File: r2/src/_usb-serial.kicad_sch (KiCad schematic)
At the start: 8 parts

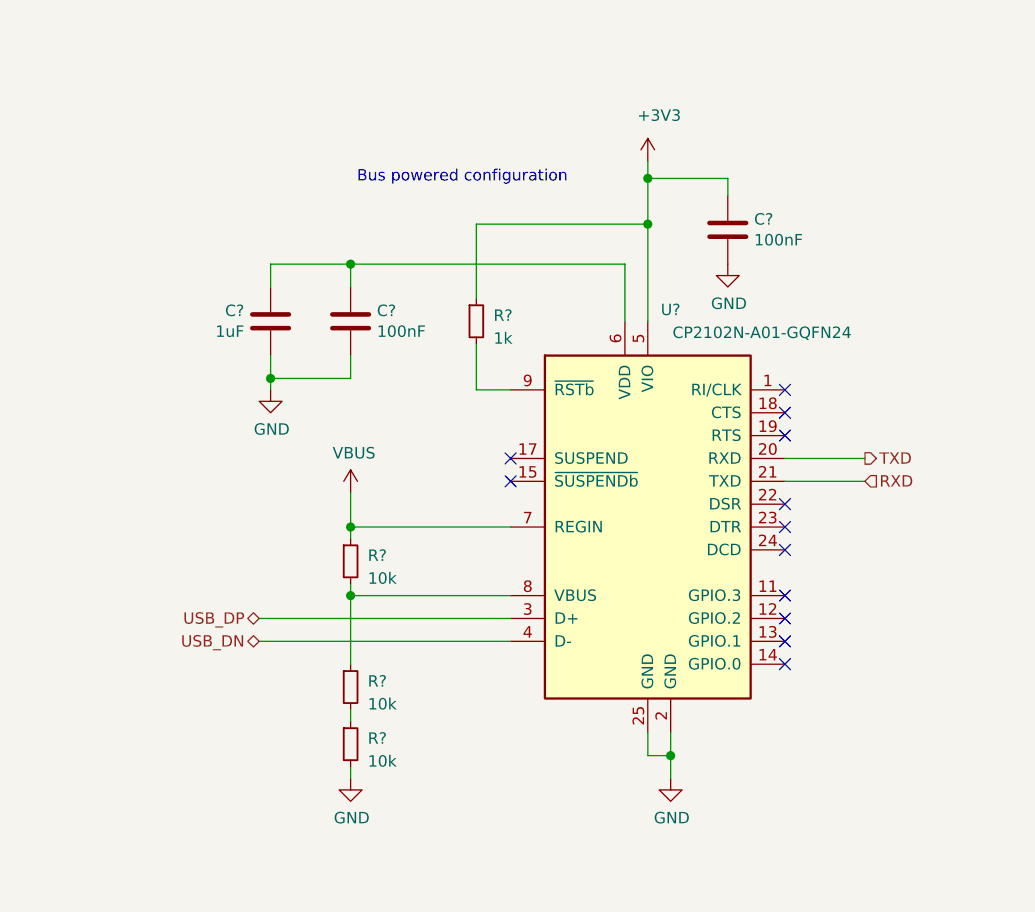
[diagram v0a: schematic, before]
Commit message: Annotate schematic, ERC pass
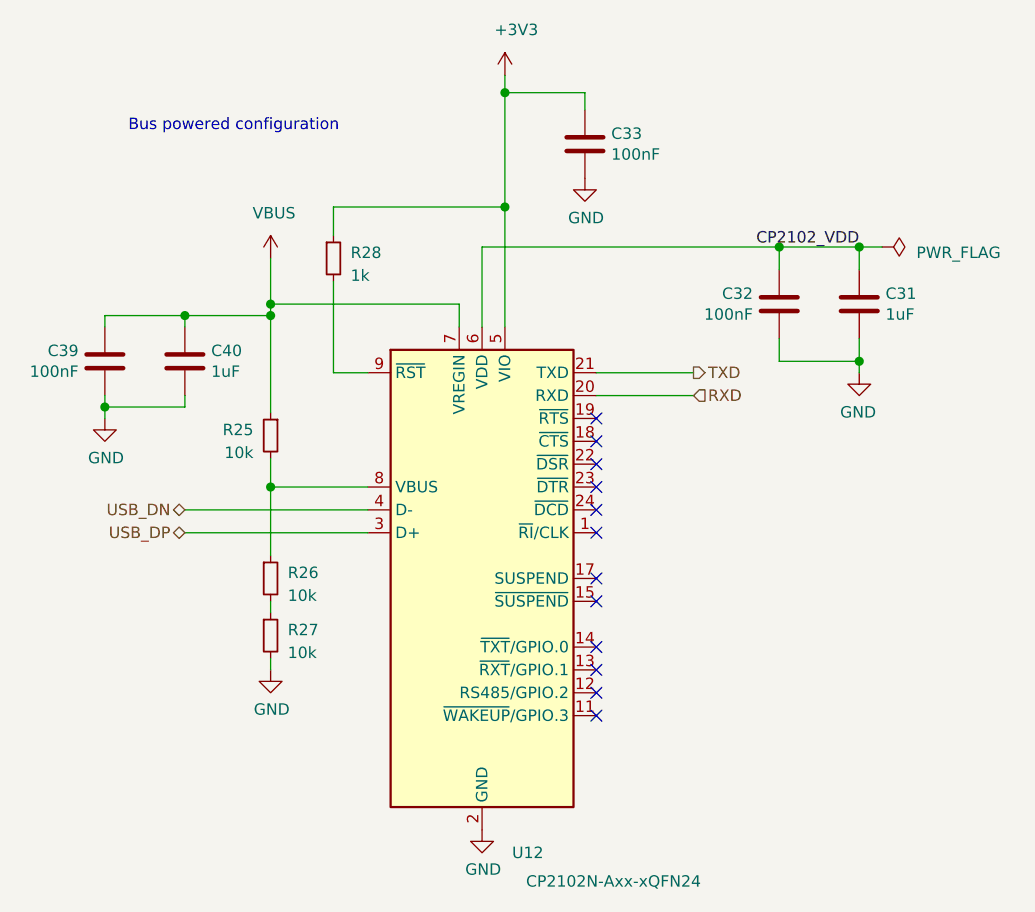
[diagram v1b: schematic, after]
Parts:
- removed U?: CP2102N-A01-GQFN24, Package_DFN_QFN:QFN-24-1EP_4x4mm_P0.5mm_EP2.6x2.6mm, symbol Interface_USB:CP2102N-A01-GQFN24
- added C39: 100nF, Capacitor_SMD:C_0402_1005Metric, symbol Device:C
- added C40: 1uF, Capacitor_SMD:C_0603_1608Metric, symbol Device:C
- added U12: CP2102N-Axx-xQFN24, Package_DFN_QFN:QFN-24-1EP_4x4mm_P0.5mm_EP2.6x2.6mm, symbol Interface_USB:CP2102N-Axx-xQFN24
- gave numbers to parts that had none: 7
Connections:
- net +3V3: now also U12.5 (VIO)
- net GND: now also C39.2, C40.2, U12.2 (GND), U12.25 (GND)
- net RXD: now also U12.20 (RXD)
- net TXD: now also U12.21 (TXD)
- net USB_DN: now also U12.4 (D-)
- net USB_DP: now also U12.3 (D+)
- net VBUS: now also C39.1, C40.1, U12.7 (VREGIN)
- net CP2102_VDD: now reaches C31.1, C32.1
- net CP2102_VDD: now also U12.6 (VDD)
- net at R25.2, R26.1: now also U12.8 (VBUS)
- net at R28.2: now also U12.9 (~RST)
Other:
- moved on the sheet: C31, C32, C33, R25, R26, R27, R28

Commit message: Most footprints assigned
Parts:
- C32, C33, C39: footprint Capacitor_SMD:C_0402_1005Metric -> Capacitor_SMD:C_0603_1608Metric
- R25, R26, R27: value 10k -> 23.7k; footprint (none) -> Resistor_SMD:R_0603_1608Metric
- R28: footprint (none) -> Resistor_SMD:R_0603_1608Metric
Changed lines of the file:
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@@
     (pin "1")
   )
-  (symbol (lib_id "Device:R_Small") (at 119.38 93.98 0) (mirror y) (unit 1)
+  (symbol (lib_id "Device:R_Small") (at 119.38 93.98 0) (unit 1)
     (in_bom yes) (on_board yes)
-    (property "Reference" "R25" (id 0) (at 117.475 93.345 0)
+    (property "Reference" "R25" (id 0) (at 121.285 93.345 0)
       (effects (font (size 1.27 1.27)) (justify left))
     )
-    (property "Value" "10k" (id 1) (at 117.475 95.885 0)
+    (property "Value" "23.7k" (id 1) (at 121.285 95.885 0)
       (effects (font (size 1.27 1.27)) (justify left))
     )
-    (property "Footprint" "" (id 2) (at 119.38 93.98 0)
+    (property "Footprint" "Resistor_SMD:R_0603_1608Metric" (id 2) (at 119.38 93.98 0)
       (effects (font (size 1.27 1.27)) hide)
     )
@@
       (effects (font (size 1.27 1.27)) (justify left))
     )
-    (property "Value" "10k" (id 1) (at 121.285 111.76 0)
+    (property "Value" "23.7k" (id 1) (at 121.285 111.76 0)
       (effects (font (size 1.27 1.27)) (justify left))
     )
-    (property "Footprint" "" (id 2) (at 119.38 109.855 0)
+    (property "Footprint" "Resistor_SMD:R_0603_1608Metric" (id 2) (at 119.38 109.855 0)
       (effects (font (size 1.27 1.27)) hide)
     )
@@
       (effects (font (size 1.27 1.27)) (justify left))
     )
-    (property "Value" "10k" (id 1) (at 121.285 118.11 0)
+    (property "Value" "23.7k" (id 1) (at 121.285 118.11 0)
       (effects (font (size 1.27 1.27)) (justify left))
     )
-    (property "Footprint" "" (id 2) (at 119.38 116.205 0)
+    (property "Footprint" "Resistor_SMD:R_0603_1608Metric" (id 2) (at 119.38 116.205 0)
       (effects (font (size 1.27 1.27)) hide)
     )
@@
       (effects (font (size 1.27 1.27)) (justify left))
     )
-    (property "Footprint" "" (id 2) (at 126.365 74.295 0)
+    (property "Footprint" "Resistor_SMD:R_0603_1608Metric" (id 2) (at 126.365 74.295 0)
       (effects (font (size 1.27 1.27)) hide)
     )
@@
       (effects (font (size 1.27 1.27)) (justify left))
     )
-    (property "Footprint" "Capacitor_SMD:C_0402_1005Metric" (id 2) (at 99.9998 89.535 0)
+    (property "Footprint" "Capacitor_SMD:C_0603_1608Metric" (id 2) (at 99.9998 89.535 0)
       (effects (font (size 1.27 1.27)) hide)
     )
@@
       (effects (font (size 1.27 1.27)) (justify left))
     )
-    (property "Footprint" "Capacitor_SMD:C_0402_1005Metric" (id 2) (at 155.2702 65.405 0)
+    (property "Footprint" "Capacitor_SMD:C_0603_1608Metric" (id 2) (at 155.2702 65.405 0)
       (effects (font (size 1.27 1.27)) hide)
     )
@@
       (effects (font (size 1.27 1.27)) (justify left))
     )
-    (property "Footprint" "Capacitor_SMD:C_0402_1005Metric" (id 2) (at 174.9298 83.185 0)
+    (property "Footprint" "Capacitor_SMD:C_0603_1608Metric" (id 2) (at 174.9298 83.185 0)
       (effects (font (size 1.27 1.27)) hide)
     )
